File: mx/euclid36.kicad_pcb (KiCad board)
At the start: 2 copper layers, 248.2 x 127 mm, 95 parts, among them SW10 SW_PUSH, SW11 SW_PUSH, SW12 SW_PUSH, SW14 SW_PUSH, SW15 SW_PUSH, SW16 SW_PUSH, SW17 SW_PUSH, SW18 SW_PUSH, SW19 SW_PUSH, SW2 SW_PUSH, SW20 SW_PUSH, SW21 SW_PUSH, SW22 SW_PUSH, SW23 SW_PUSH, SW25 SW_PUSH, SW26 SW_PUSH, SW27 SW_PUSH, SW28 SW_PUSH, SW29 SW_PUSH, SW3 SW_PUSH, SW31 SW_PUSH, SW32 SW_PUSH, SW33 SW_PUSH, SW34 SW_PUSH, SW35 SW_PUSH, SW37 SW_PUSH, SW38 SW_PUSH, SW39 SW_PUSH, SW4 SW_PUSH, SW40 SW_PUSH, SW41 SW_PUSH, SW42 SW_PUSH, SW5 SW_PUSH, SW6 SW_PUSH, SW8 SW_PUSH, SW9 SW_PUSH, U1 ProMicro

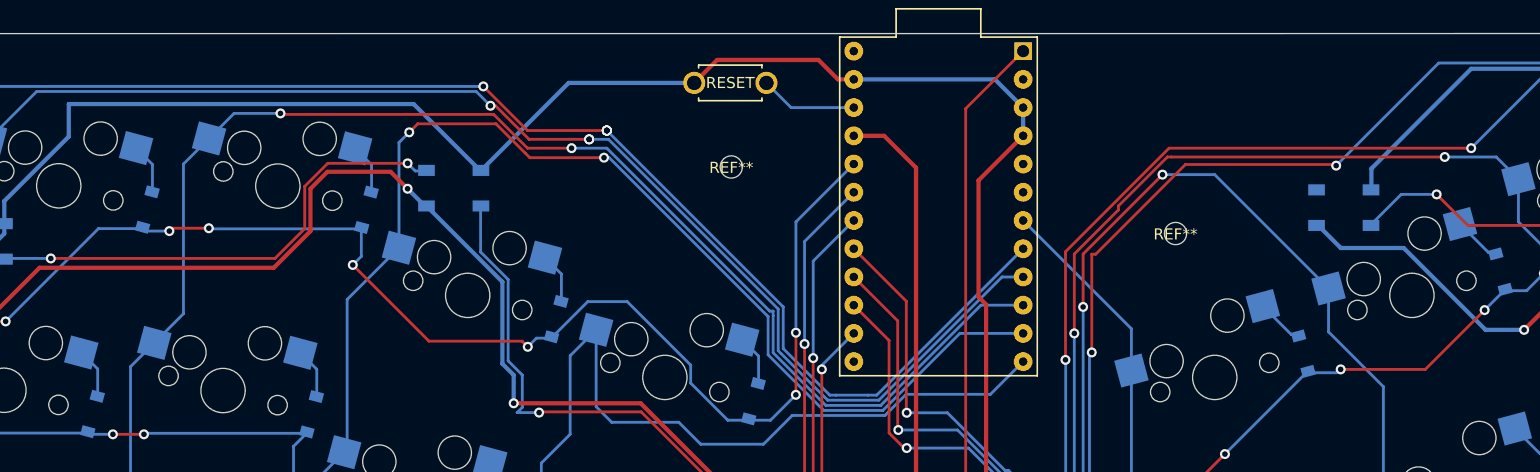
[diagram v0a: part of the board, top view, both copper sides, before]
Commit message: moved 2 LEDs slightly up as they were overlapping with hotswap sockets
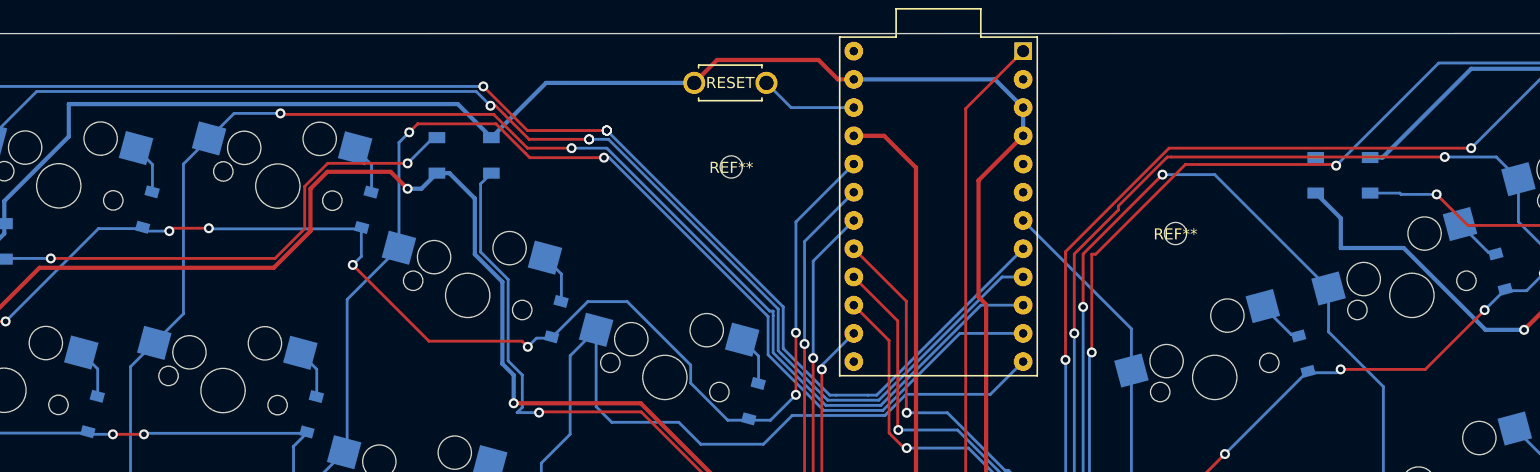
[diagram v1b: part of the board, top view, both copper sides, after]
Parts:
- moved L4 3.10 mm to (107.8, 36.4)
- moved L13 2.91 mm to (186.9, 38.2)
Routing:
- net VCC: track 695.5 -> 702.5 mm
- net GND: track 642.0 -> 637.4 mm
- net Net-(L3-Pad2): track 93.2 -> 96.6 mm
- net Net-(L4-Pad2): track 44.1 -> 45.7 mm
- net Net-(L12-Pad2): track 47.8 -> 46.8 mm

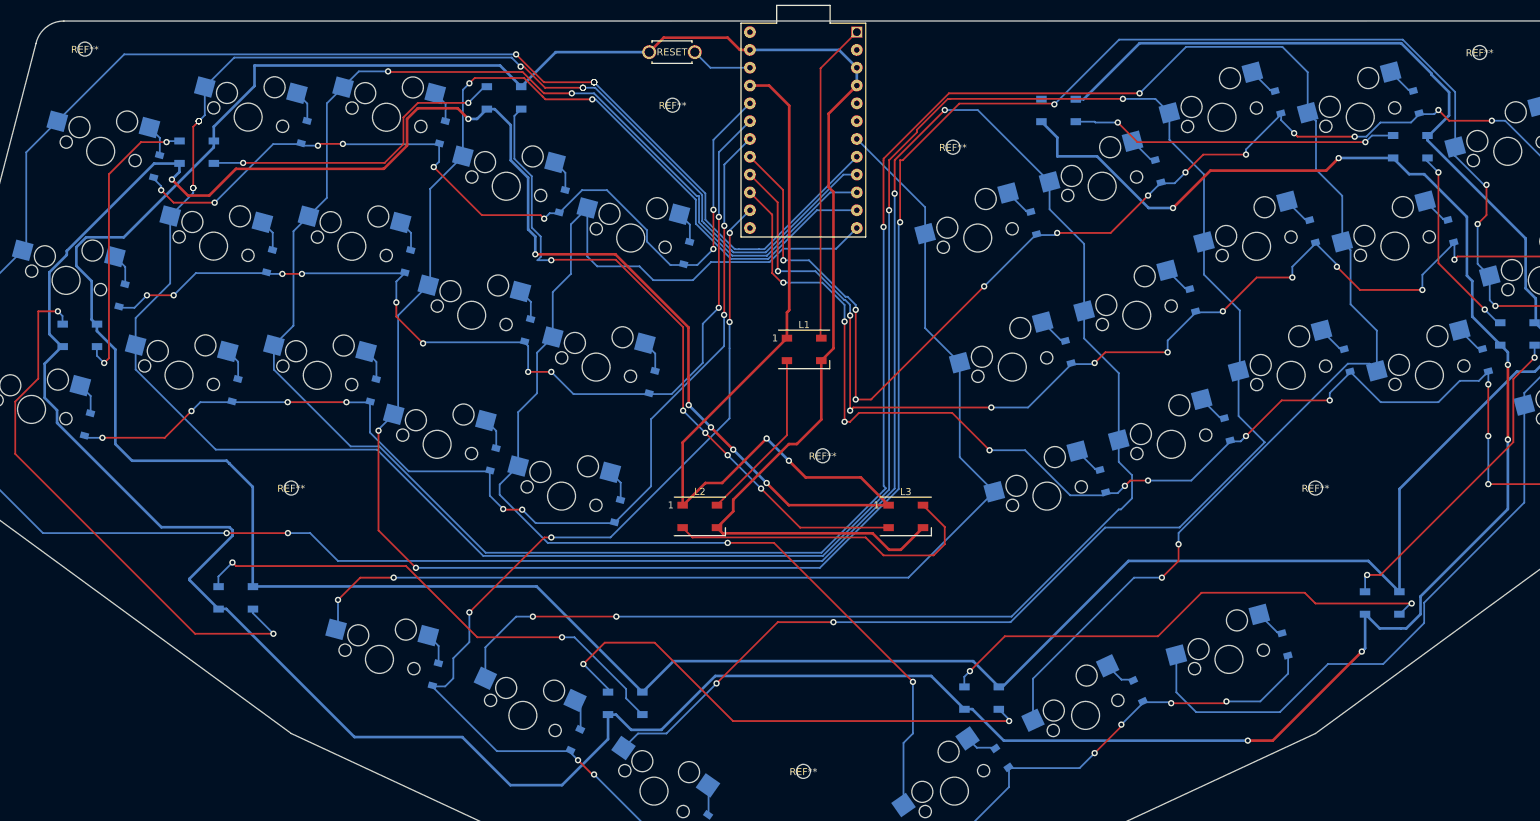
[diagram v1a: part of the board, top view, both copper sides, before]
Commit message: added mx sandwich case and updated pcb to support OLED
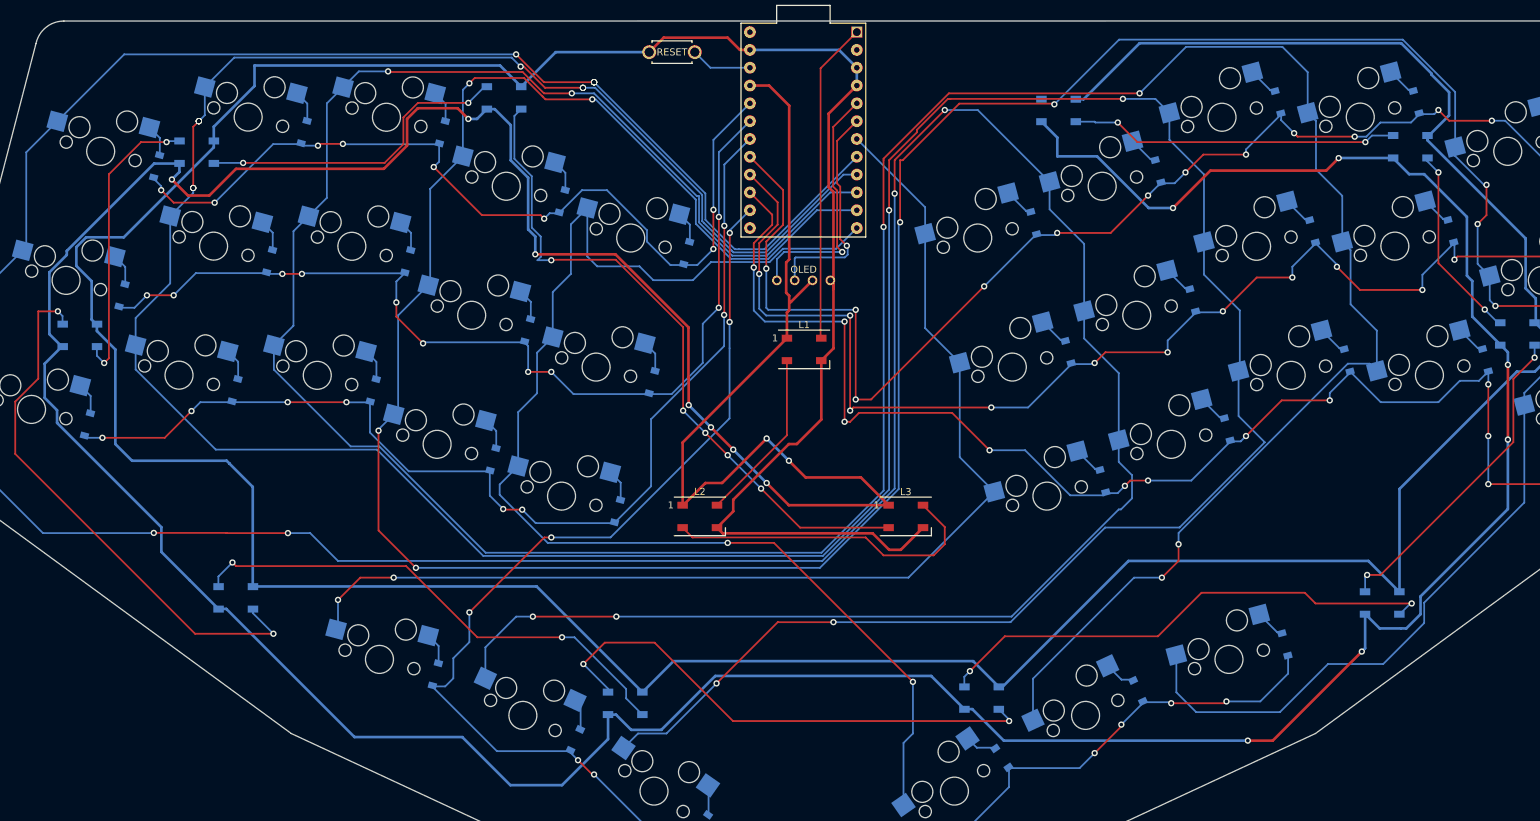
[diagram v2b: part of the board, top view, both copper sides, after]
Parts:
- removed REF** (x8): M2_Hole_NPTH_Outside, _reviung-kbd:M2_Hole_NPTH_Outside
- added OL1: OLED, _reviung-kbd:OLED_v2, F.Cu at (150.5, 62.4)
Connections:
- U1 pad 5: Net-(U1-Pad5) -> SDA
- U1 pad 6: Net-(U1-Pad6) -> SCL
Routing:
- net SDA: track 0.00 -> 35.9 mm, vias 0 -> 1
- net SCL: track 0.00 -> 31.7 mm, vias 0 -> 1
- net row3: track 168.9 -> 175.8 mm
- net row4: track 174.3 -> 180.3 mm
- net VCC: track 702.5 -> 696.7 mm
- net row5: track 193.6 -> 199.1 mm
- net GND: track 637.4 -> 638.8 mm
